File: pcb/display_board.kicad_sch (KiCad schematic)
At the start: 56 parts, among them J301 TO_MAIN, SW301 SAMPLE RATE, SW302 LOOPBACK, U301 HT1635D

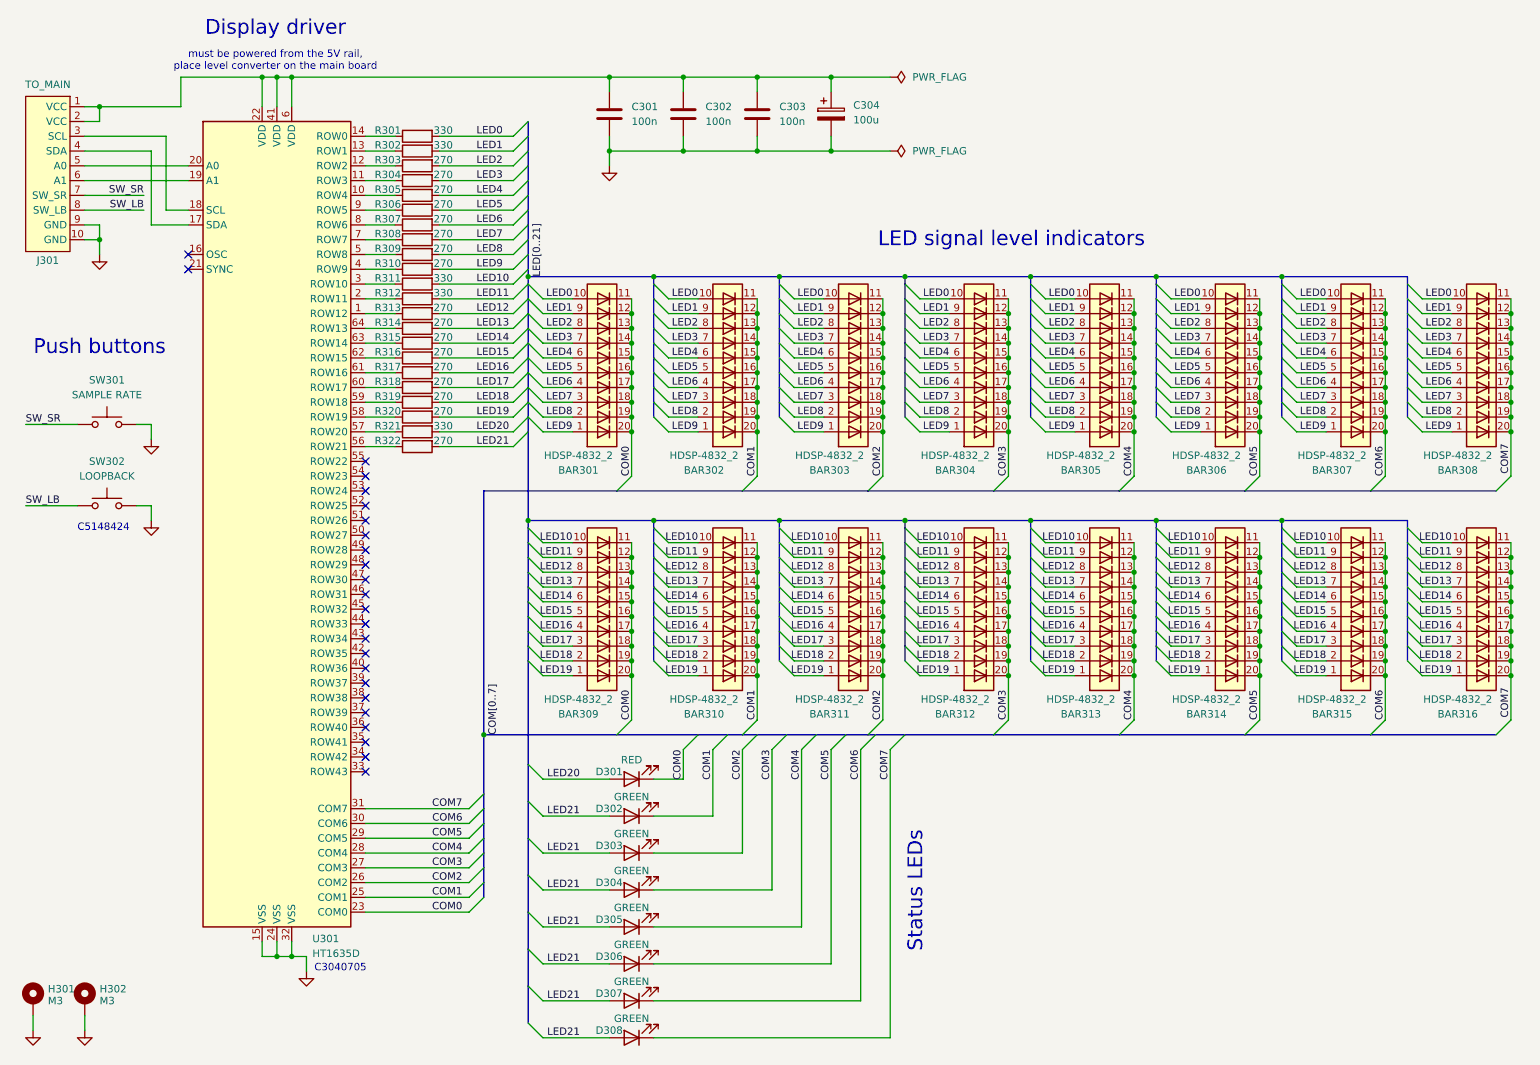
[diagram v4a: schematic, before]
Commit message: Draw first version of display board
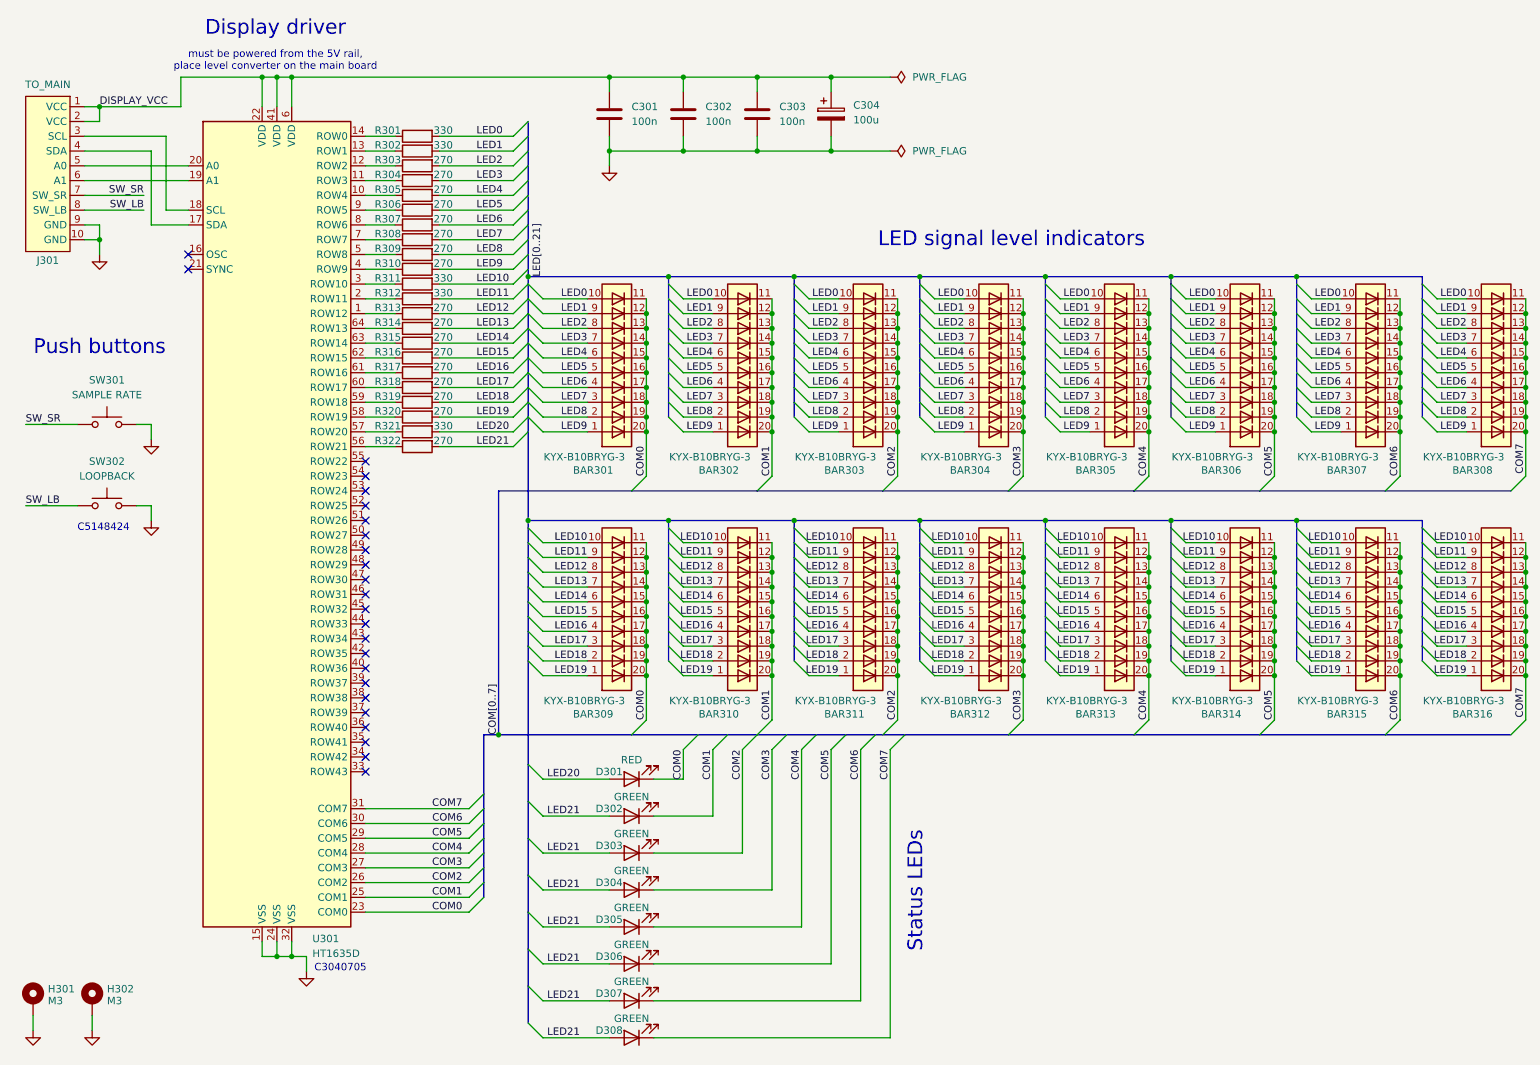
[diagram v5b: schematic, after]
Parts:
- BAR301, BAR302, BAR303, BAR304, BAR305, BAR306, BAR307, BAR308, BAR309, BAR310, BAR311, BAR312, BAR313, BAR314, BAR315, BAR316: value HDSP-4832_2 -> KYX-B10BRYG-3; footprint Display:HDSP-4832 -> adatv2:LED_10bar
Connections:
- net DISPLAY_VCC: now reaches C301.1, C302.1, C303.1, C304.1, J301.1 (VCC), J301.2 (VCC), U301.22 (VDD), U301.41 (VDD), U301.6 (VDD)
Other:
- moved on the sheet: BAR301, BAR302, BAR303, BAR304, BAR305, BAR306, BAR307, BAR308, BAR309, BAR310, BAR311, BAR312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
